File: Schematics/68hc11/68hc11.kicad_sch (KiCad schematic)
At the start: 4 parts

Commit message: Start wiring components
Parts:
- removed U?: MC68B21, Package_DIP:DIP-40_W15.24mm, symbol Interface:MC68B21
- U2, U3: renamed from U?; footprint (none) -> Package_DIP:DIP-20_W7.62mm_Socket
- gave numbers to parts that had none: 1
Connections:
- net +5V: now also U1.26 (VDD), U2.20 (VCC), U3.20 (VCC)
- net GND: now also U1.1 (VSS), U2.10 (GND), U3.1 (OE), U3.10 (GND)
- net at U3.11 (LE): now also U1.4 (AS), U2.19 (CE)
- net A4: now reaches U3.12 (O4)
- net AD4: now reaches U3.13 (D4)
- net AD4: now also U1.13 (AD4/PC4), U2.14 (B4)
- net AD5: now reaches U3.14 (D5)
- net AD5: now also U1.14 (AD5/PC5), U2.13 (B5)
- net A5: now reaches U3.15 (O5)
- net A6: now reaches U3.16 (O6)
- net AD6: now reaches U3.17 (D6)
- net AD6: now also U1.15 (AD6/PC6), U2.12 (B6)
- net AD7: now reaches U3.18 (D7)
- net AD7: now also U1.16 (AD7/PC7), U2.11 (B7)
- net A7: now reaches U3.19 (O7)
- net A0: now reaches U3.2 (O0)
- net AD0: now reaches U3.3 (D0)
- net AD0: now also U1.9 (AD0/PC0), U2.18 (B0)
- net AD1: now reaches U3.4 (D1)
- net AD1: now also U1.10 (AD1/PC1), U2.17 (B1)
- net A1: now reaches U3.5 (O1)
- net A2: now reaches U3.6 (O2)
- net AD2: now reaches U3.7 (D2)
- net AD2: now also U1.11 (AD2/PC2), U2.16 (B2)
- net AD3: now reaches U3.8 (D3)
- net AD3: now also U1.12 (AD3/PC3), U2.15 (B3)
- net A3: now reaches U3.9 (O3)
- net A15: now reaches U1.35 (A15/PB7)
- net A14: now reaches U1.36 (A14/PB6)
- net A13: now reaches U1.37 (A13/PB5)
- net A12: now reaches U1.38 (A12/PB4)
- net A11: now reaches U1.39 (A11/PB3)
- net A10: now reaches U1.40 (A10/PB2)
- net A9: now reaches U1.41 (A9/PB1)
- net A8: now reaches U1.42 (A8/PB0)
- net at U1.6 (R/W): now also U2.1 (A->B)
- net D0: now reaches U2.2 (A0)
- net D1: now reaches U2.3 (A1)
- net D2: now reaches U2.4 (A2)
- net D3: now reaches U2.5 (A3)
- net D4: now reaches U2.6 (A4)
- net D5: now reaches U2.7 (A5)
- net D6: now reaches U2.8 (A6)
- net D7: now reaches U2.9 (A7)
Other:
- moved on the sheet: U2, U3

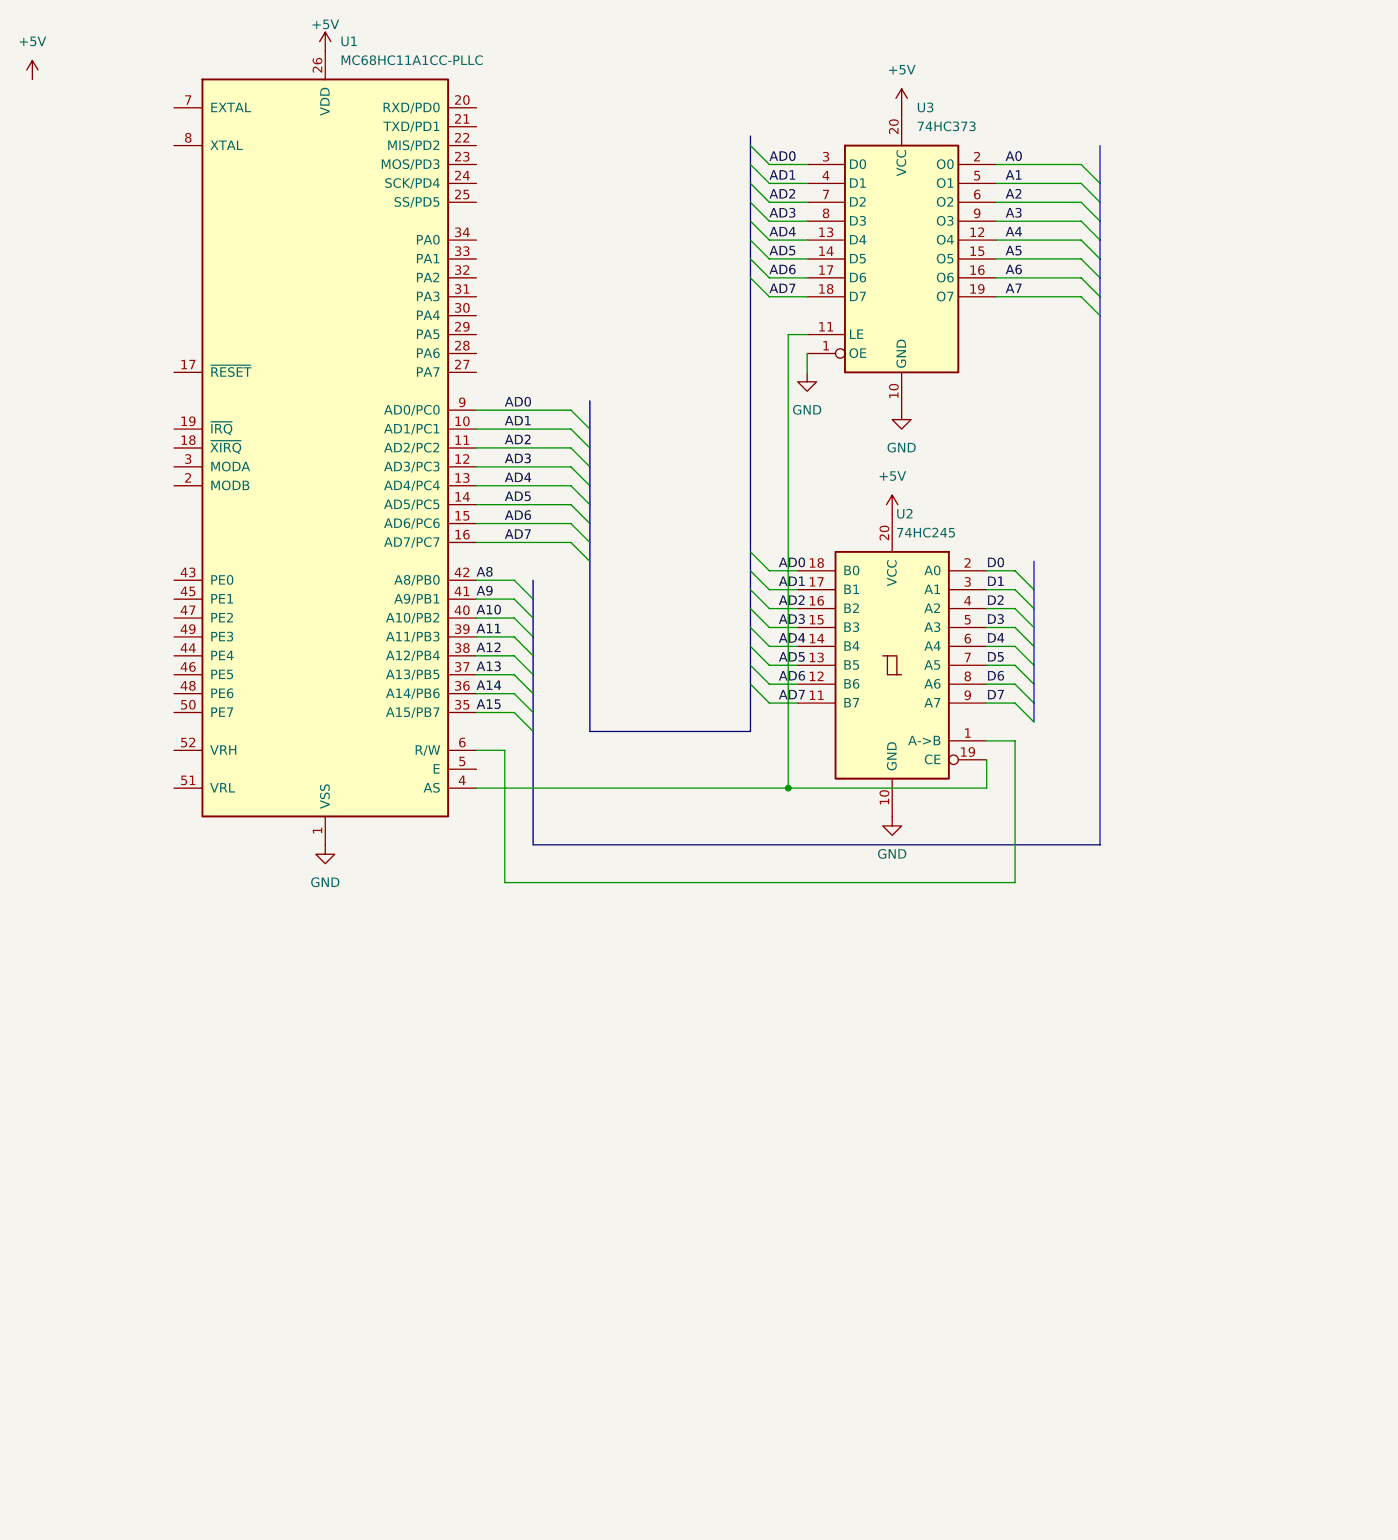
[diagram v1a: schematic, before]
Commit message: Added some more chips to design
Need to finish Addres block decoding soon.
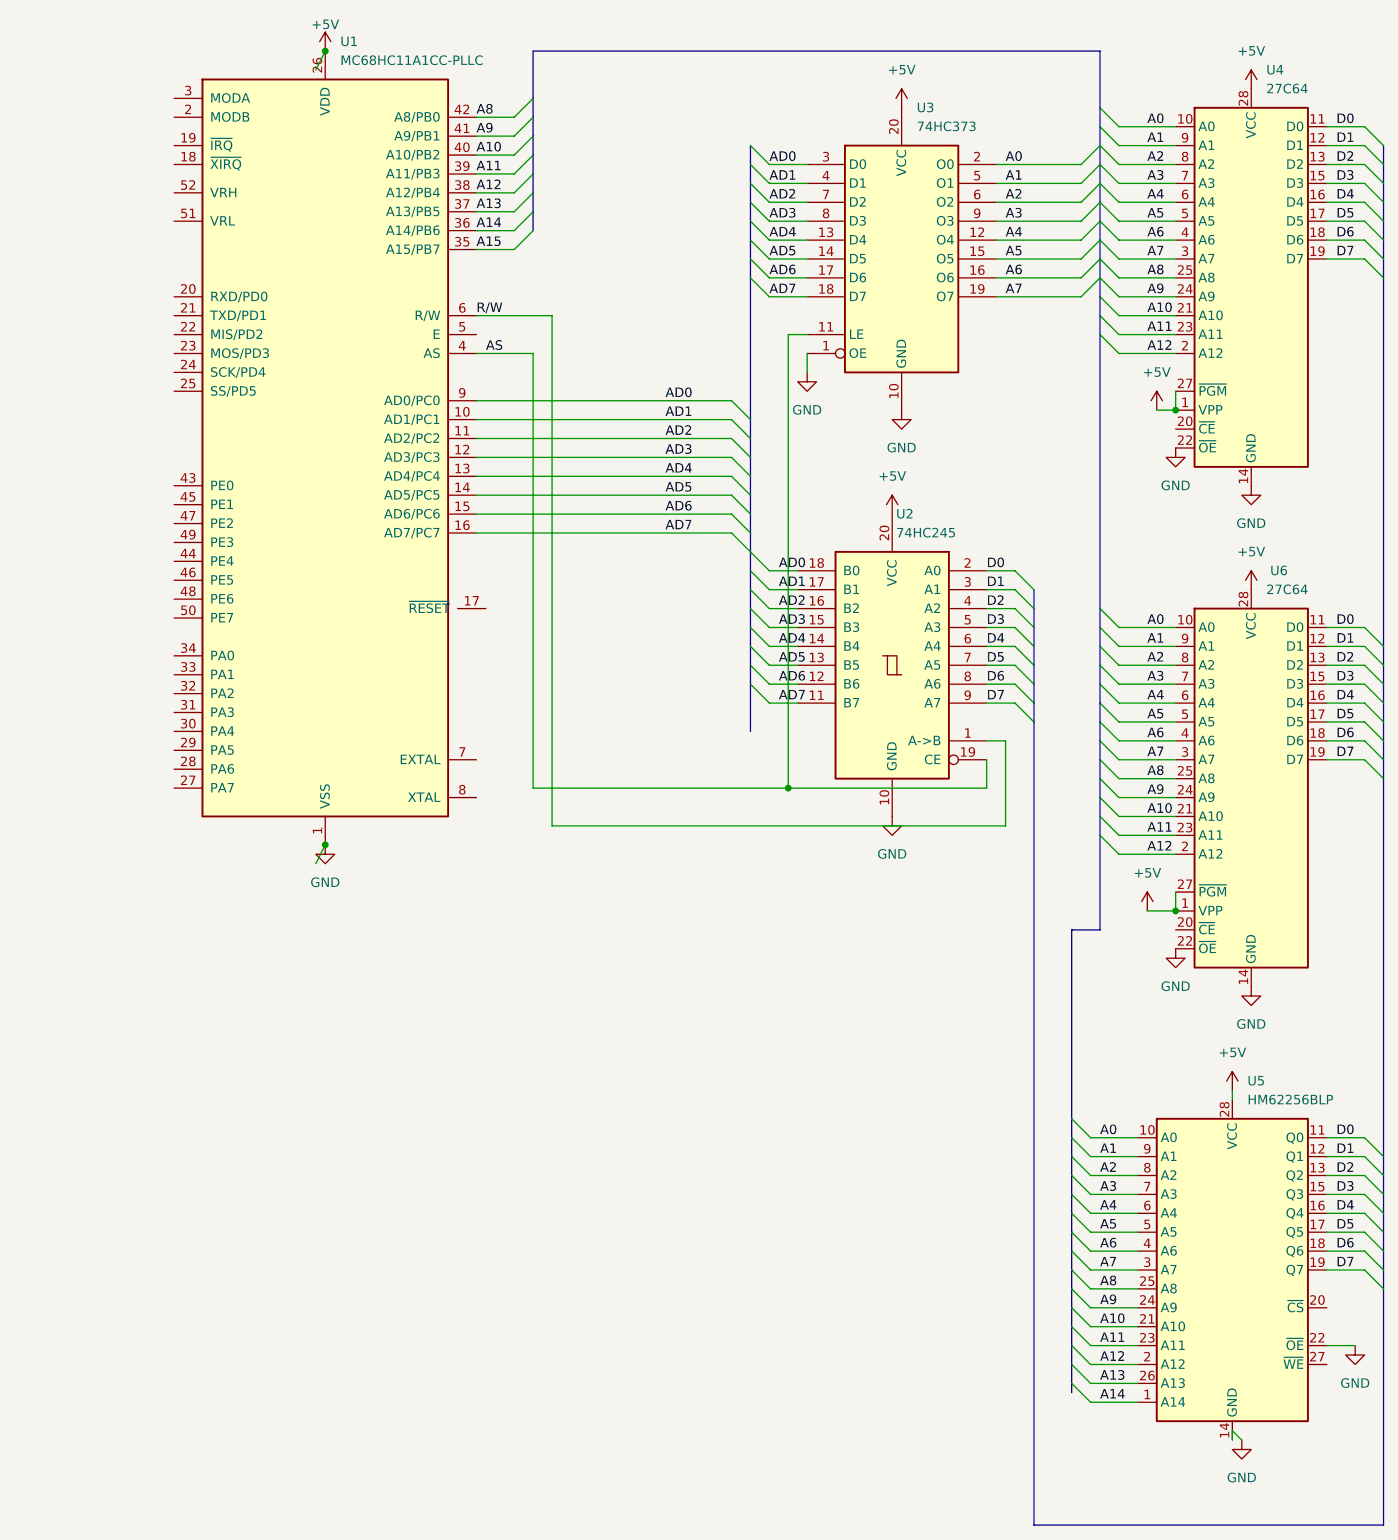
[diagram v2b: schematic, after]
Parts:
- added U4, U6: 27C64, Package_DIP:DIP-28_W15.24mm, symbol Memory_EPROM:27C64
- added U5: HM62256BLP, Package_DIP:DIP-28_W15.24mm, symbol Memory_RAM:HM62256BLP
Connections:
- net +5V: now also U4.1 (VPP), U4.27 (~{PGM}), U4.28 (VCC), U5.28 (VCC), U6.1 (VPP), U6.27 (~{PGM}), U6.28 (VCC)
- net A0: now also U4.10 (A0), U5.10 (A0), U6.10 (A0)
- net A1: now also U4.9 (A1), U5.9 (A1), U6.9 (A1)
- net A10: now also U4.21 (A10), U5.21 (A10), U6.21 (A10)
- net A11: now also U4.23 (A11), U5.23 (A11), U6.23 (A11)
- net A12: now also U4.2 (A12), U5.2 (A12), U6.2 (A12)
- net A13: now also U5.26 (A13)
- net A14: now also U5.1 (A14)
- net A2: now also U4.8 (A2), U5.8 (A2), U6.8 (A2)
- net A3: now also U4.7 (A3), U5.7 (A3), U6.7 (A3)
- net A4: now also U4.6 (A4), U5.6 (A4), U6.6 (A4)
- net A5: now also U4.5 (A5), U5.5 (A5), U6.5 (A5)
- net A6: now also U4.4 (A6), U5.4 (A6), U6.4 (A6)
- net A7: now also U4.3 (A7), U5.3 (A7), U6.3 (A7)
- net A8: now also U4.25 (A8), U5.25 (A8), U6.25 (A8)
- net A9: now also U4.24 (A9), U5.24 (A9), U6.24 (A9)
- net D0: now also U4.11 (D0), U5.11 (Q0), U6.11 (D0)
- net D1: now also U4.12 (D1), U5.12 (Q1), U6.12 (D1)
- net D2: now also U4.13 (D2), U5.13 (Q2), U6.13 (D2)
- net D3: now also U4.15 (D3), U5.15 (Q3), U6.15 (D3)
- net D4: now also U4.16 (D4), U5.16 (Q4), U6.16 (D4)
- net D5: now also U4.17 (D5), U5.17 (Q5), U6.17 (D5)
- net D6: now also U4.18 (D6), U5.18 (Q6), U6.18 (D6)
- net D7: now also U4.19 (D7), U5.19 (Q7), U6.19 (D7)
- net GND: now also U4.14 (GND), U4.22 (~{OE}), U5.14 (GND), U5.22 (~{OE}), U6.14 (GND), U6.22 (~{OE})
- net AS: now reaches U1.4 (AS), U2.19 (CE), U3.11 (LE)
- net R/W: now reaches U1.6 (R/W), U2.1 (A->B)
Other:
- title: (none) -> MC68HC11 SBC Eval Board
- moved on the sheet: U1

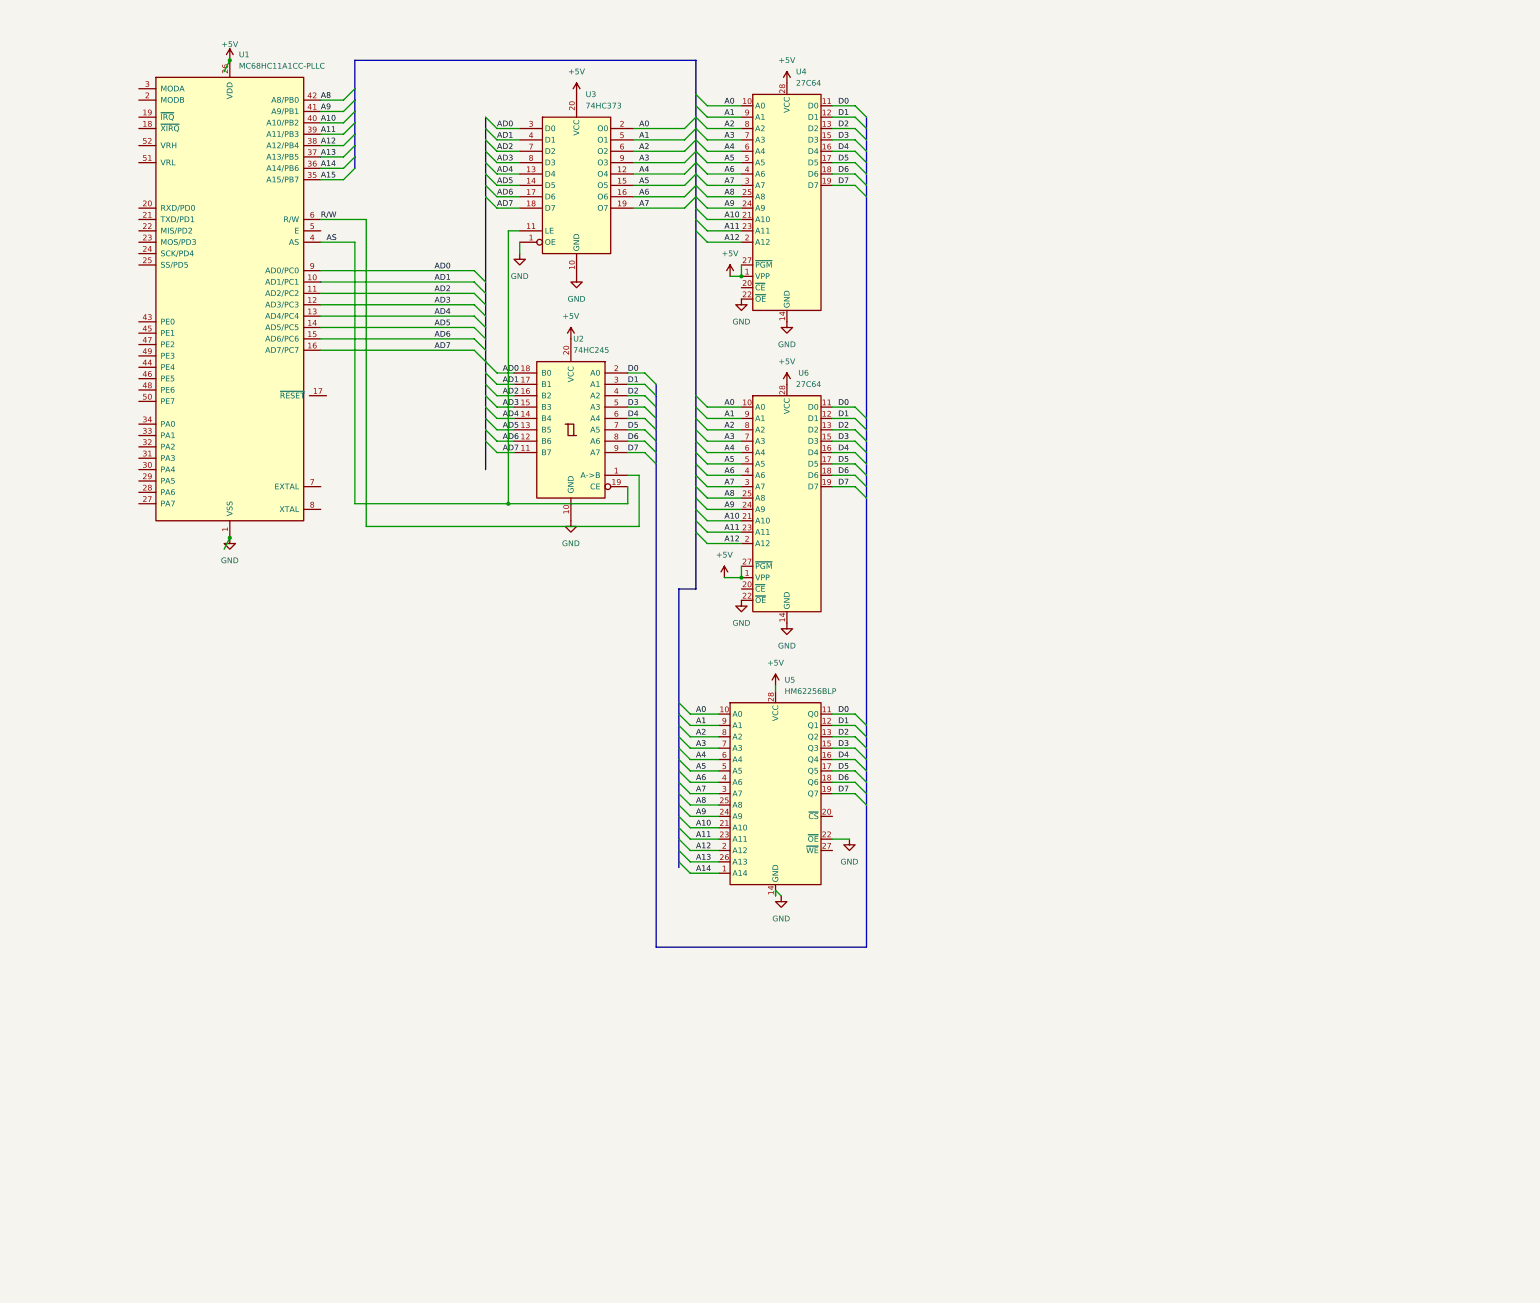
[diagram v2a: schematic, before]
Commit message: Added more components to schematic
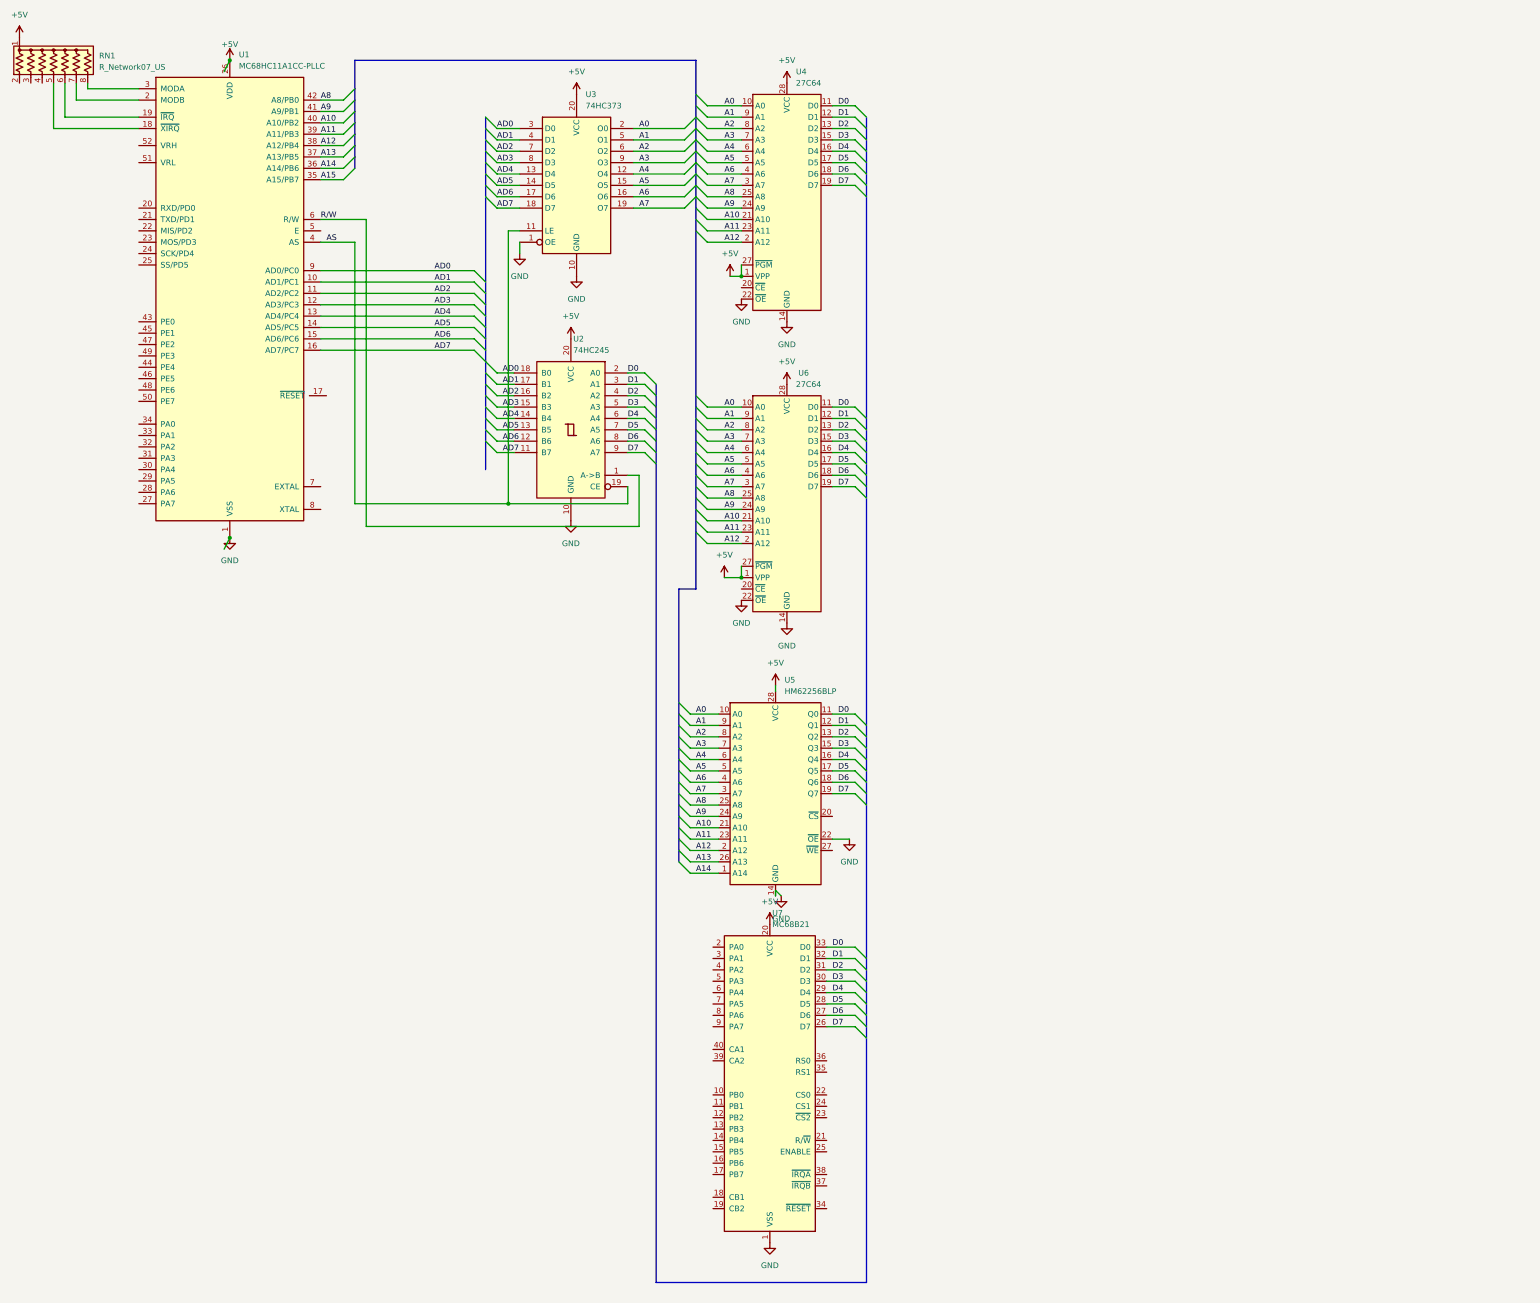
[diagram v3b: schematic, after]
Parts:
- added RN1: R_Network07_US, Resistor_THT:R_Array_SIP8, symbol Device:R_Network07_US
- added U7: MC68B21, Package_DIP:DIP-40_W15.24mm, symbol Interface:MC68B21
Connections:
- net +5V: now also RN1.1 (common), U7.20 (VCC)
- net D0: now also U7.33 (D0)
- net D1: now also U7.32 (D1)
- net D2: now also U7.31 (D2)
- net D3: now also U7.30 (D3)
- net D4: now also U7.29 (D4)
- net D5: now also U7.28 (D5)
- net D6: now also U7.27 (D6)
- net D7: now also U7.26 (D7)
- net GND: now also U7.1 (VSS)
- net at U1.18 (~{XIRQ}): now also RN1.5 (R4)
- net at U1.19 (~{IRQ}): now also RN1.6 (R5)
- net at U1.2 (MODB): now also RN1.7 (R6)
- net at U1.3 (MODA): now also RN1.8 (R7)
